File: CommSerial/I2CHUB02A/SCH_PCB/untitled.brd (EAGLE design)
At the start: 50.3 x 40.1 mm, 65 parts, among them X2 SROUB3M, X3 SROUB3M, X4 SROUB3M, X5 SROUB3M, X6 LM1117-3.3

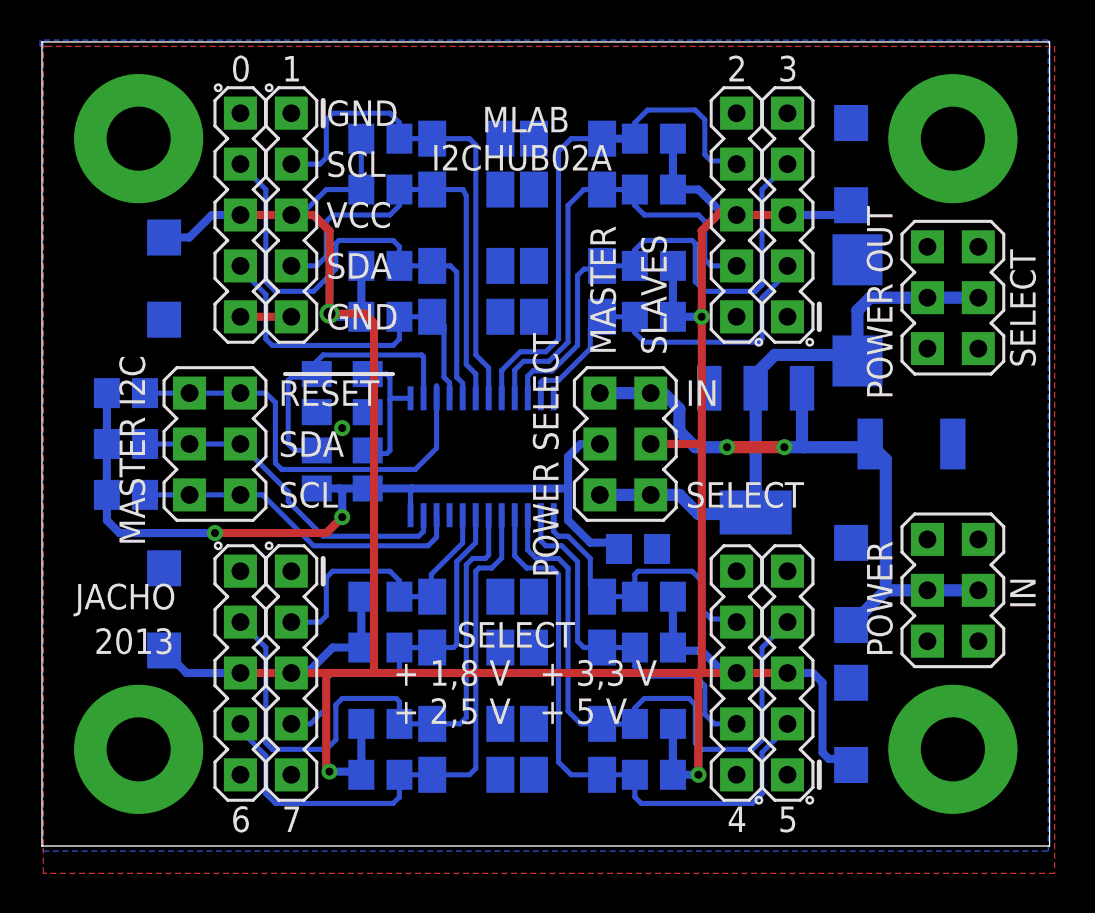
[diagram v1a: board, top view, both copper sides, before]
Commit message: 
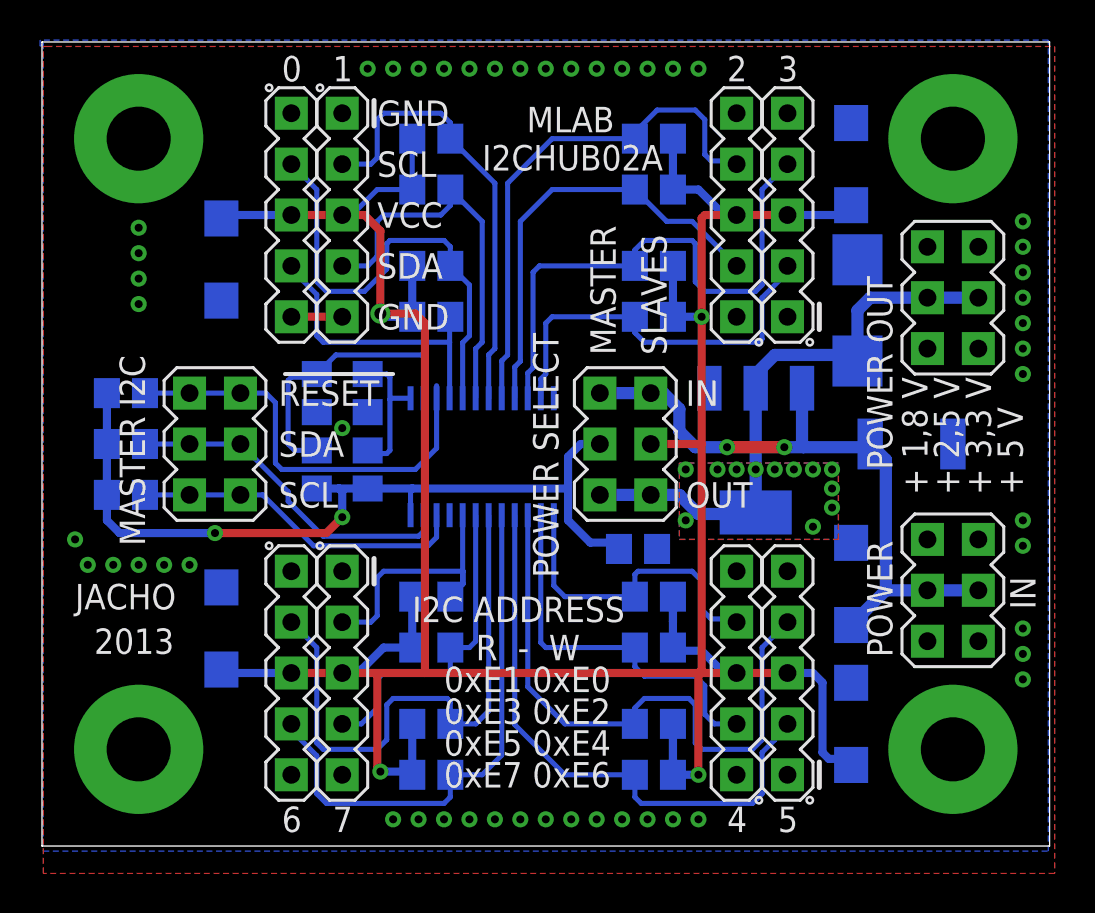
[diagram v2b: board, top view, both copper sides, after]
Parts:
- removed D11, D12, D14, D15, D17, D18, D2, D20, D21, D23, D24, D3, D5, D6, D8, D9: ZD, moje_diody:MINIMELF
- moved D4 3.01 mm to (9.21, 29.5)
- moved D10 3.01 mm to (9.21, 11.1)
- moved SV2 2.54 mm to (15.2, 31.8)
- moved SV8 2.54 mm to (15.2, 8.89)
- moved R1 2.54 mm to (19.7, 29.2)
- moved R13 2.54 mm to (19.7, 6.35)
- moved R14 2.54 mm to (19.7, 3.81)
- moved R15 2.54 mm to (19.7, 12.7)
- moved R16 2.54 mm to (19.7, 10.2)
- moved R2 2.54 mm to (19.7, 26.7)
- moved R3 2.54 mm to (19.7, 35.6)
- moved R4 2.54 mm to (19.7, 33.0)
- moved SV1 2.54 mm to (12.7, 31.8)
- moved SV7 2.54 mm to (12.7, 8.89)
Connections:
- net GND: no longer D11.A, D12.A, D14.A, D15.A, D17.A, D18.A, D2.A, D20.A, D21.A, D23.A, D24.A, D3.A, D5.A, D6.A, D8.A, D9.A
- net SC0: no longer D3.C
- net SC1: no longer D6.C
- net SC2: no longer D9.C
- net SC3: no longer D12.C
- net SC4: no longer D15.C
- net SC5: no longer D18.C
- net SC6: no longer D21.C
- net SC7: no longer D24.C
- net SD0: no longer D2.C
- net SD1: no longer D5.C
- net SD2: no longer D8.C
- net SD3: no longer D11.C
- net SD4: no longer D14.C
- net SD5: no longer D17.C
- net SD6: no longer D20.C
- net SD7: no longer D23.C
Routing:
- net SD0: track 19.2 -> 14.9 mm
- net +V1: track 160.5 -> 157.3 mm
- net SC0: track 26.2 -> 23.3 mm
- net SC1: track 25.4 -> 22.6 mm
- net SD6: track 29.9 -> 27.1 mm
- net SD1: track 22.3 -> 19.7 mm
- net SC6: track 31.0 -> 28.6 mm
- net SD7: track 18.5 -> 16.2 mm
- net SC7: track 15.1 -> 13.3 mm
- net SC2: track 23.4 -> 22.0 mm
- net SC5: track 30.4 -> 29.3 mm
- net SC3: track 19.0 -> 20.0 mm
- net SD4: track 15.1 -> 15.9 mm
- net SD3: track 27.0 -> 27.8 mm
- net SC4: track 18.6 -> 19.2 mm
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- added copper zone on layer 1, net +3.3V
- added copper zone on layer 16, net +3.3V
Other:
- board text added: "0xE1 0xE0"
- board text added: "0xE3 0xE2"
- board text added: "0xE5 0xE4"
- board text added: "0xE7 0xE6"
- board text added: "I2C ADDRESS"
- board text added: "OUT"
- board text added: "R - W"
- board text removed: "SELECT"

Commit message: 
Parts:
- removed C4: 10uF, moje_C:B
- removed D10: TRANSIL, moje_diody:SMA
- added C1: 100nF, moje_C:C0805
- added D5: M4, moje:SMA
- C2: value 100nF -> 10uF; device moje_C:C0805 -> moje_C:B
- D1: value (none) -> SMBJ5.0A; device moje:SMA -> moje_diody:SMA
- D2, D3, D4: value TRANSIL -> SMBJ5.0A
- R1, R17, R18, R19, R2: value 4k7 -> 10k
- R10, R11, R12, R13, R14, R15, R16, R3, R4, R5, R6, R7, R8, R9: value (none) -> 10k
- X1: value (none) -> TCA9548A
- moved D1 31.5 mm to (9.21, 11.1)
- moved C2 14.8 mm to (43.8, 20.3), turned to 0 degrees
- renumbered D16 to D2, D22 to D3
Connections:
- net +V1: now also D1.K; no longer D10.K
- net +VCC: now also C2.+, D5.K; no longer C4.+, D1.K
- net GND: now also C1.2, C2.-, D5.A; no longer C2.2, C4.-, D10.A
- net N$5: now also C1.1; no longer C2.1
